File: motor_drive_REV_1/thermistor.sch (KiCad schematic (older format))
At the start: 6 parts, among them J5 Conn_01x02, J6 Conn_01x02

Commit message: started layout
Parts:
- removed C32, C33: 2.2uF, motor_drive_footprints:C_0603_1608Metric, symbol motor_drive:C
- removed J5: Conn_01x02, symbol Connector_Generic:Conn_01x02
- removed R44: 3k, motor_drive_footprints:C_0603_1608Metric, symbol motor_drive:R
- added C43: C, motor_drive_footprints:C_0603_1608Metric, symbol motor_drive:C
- J6: footprint (none) -> motor_drive_footprints:2pos_254
- R43: value 3k -> R
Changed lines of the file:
@@
 $Descr A4 11693 8268
 encoding utf-8
-Sheet 15 15
+Sheet 15 16
 Title ""
 Date ""
@@
 $EndDescr
 $Comp
-L motor_drive:R R44
-U 1 1 5E6227DE
-P 5400 2750
-AR Path="/5E61C379/5E6227DE" Ref="R44"  Part="1"
-AR Path="/5E61FCEC/5E6227DE" Ref="R?"  Part="1"
-AR Path="/5E626DD7/5E6227DE" Ref="R?"  Part="1"
-F 0 "R?" H 5470 2796 50  0000 L CNN
-F 1 "3k" H 5470 2705 50  0000 L CNN
-F 2 "motor_drive_footprints:C_0603_1608Metric" V 5330 2750 50  0001 C CNN
-F 3 "~" H 5400 2750 50  0001 C CNN
-	1    5400 2750
+L motor_drive:R R43
+U 1 1 5E41A8AA
+P 5500 4250
+F 0 "R43" H 5570 4296 50  0000 L CNN
+F 1 "R" H 5570 4205 50  0000 L CNN
+F 2 "motor_drive_footprints:C_0603_1608Metric" V 5430 4250 50  0001 C CNN
+F 3 "~" H 5500 4250 50  0001 C CNN
+	1    5500 4250
 	1    0    0    -1
 $EndComp
 $Comp
-L motor_drive:C C33
-U 1 1 5E6227DF
-P 4500 2750
-AR Path="/5E61C379/5E6227DF" Ref="C33"  Part="1"
-AR Path="/5E61FCEC/5E6227DF" Ref="C?"  Part="1"
-AR Path="/5E626DD7/5E6227DF" Ref="C?"  Part="1"
-F 0 "C?" H 4615 2796 50  0000 L CNN
-F 1 "2.2uF" H 4615 2705 50  0000 L CNN
-F 2 "motor_drive_footprints:C_0603_1608Metric" H 4538 2600 50  0001 C CNN
-F 3 "~" H 4500 2750 50  0001 C CNN
-	1    4500 2750
+L motor_drive:C C43
+U 1 1 5E41AB44
+P 6000 4250
+F 0 "C43" H 6115 4296 50  0000 L CNN
+F 1 "C" H 6115 4205 50  0000 L CNN
+F 2 "motor_drive_footprints:C_0603_1608Metric" H 6038 4100 50  0001 C CNN
+F 3 "~" H 6000 4250 50  0001 C CNN
+	1    6000 4250
 	1    0    0    -1
 $EndComp
 $Comp
 L Connector_Generic:Conn_01x02 J6
-U 1 1 5E6227E0
-P 5200 2200
-AR Path="/5E61C379/5E6227E0" Ref="J6"  Part="1"
-AR Path="/5E61FCEC/5E6227E0" Ref="J?"  Part="1"
-AR Path="/5E626DD7/5E6227E0" Ref="J?"  Part="1"
-F 0 "J?" H 5280 2192 50  0000 L CNN
-F 1 "Conn_01x02" H 5280 2101 50  0000 L CNN
-F 2 "" H 5200 2200 50  0001 C CNN
-F 3 "~" H 5200 2200 50  0001 C CNN
-	1    5200 2200
+U 1 1 5E41B07F
+P 6200 3700
+F 0 "J6" H 6280 3692 50  0000 L CNN
+F 1 "Conn_01x02" H 6280 3601 50  0000 L CNN
+F 2 "motor_drive_footprints:2pos_254" H 6200 3700 50  0001 C CNN
+F 3 "~" H 6200 3700 50  0001 C CNN
+	1    6200 3700
 	1    0    0    -1
 $EndComp
 Wire Wire Line
-	4500 2600 4500 2500
+	5500 3500 6000 3500
 Wire Wire Line
-	4500 2500 5000 2500
+	6000 3500 6000 3700
 Wire Wire Line
-	5000 2500 5000 2600
+	6000 3800 6000 4000
 Wire Wire Line
-	4500 2900 4500 3000
+	5500 4100 5500 4000
 Wire Wire Line
-	4500 3000 5000 3000
+	5500 4000 6000 4000
+Connection ~ 6000 4000
 Wire Wire Line
-	5000 3000 5000 2900
-Text HLabel 4500 3000 0    50   Input ~ 0
+	6000 4000 6000 4100
+Wire Wire Line
+	5500 4400 5500 4500
+Wire Wire Line
+	5500 4500 6000 4500
+Wire Wire Line
+	6000 4500 6000 4400
+Text HLabel 5500 3500 0    50   Input ~ 0
+5.0V
+Text HLabel 5500 4000 0    50   Input ~ 0
+signal
+Text HLabel 5500 4500 0    50   Input ~ 0
 GND
-Text HLabel 4500 2500 0    50   Input ~ 0
-signal
-Text HLabel 4500 2000 0    50   Input ~ 0
-5.0V
-Wire Wire Line
-	4500 2000 5000 2000
-Wire Wire Line
-	5000 2000 5000 2200
-Wire Wire Line
-	5000 2300 5000 2500
-Connection ~ 5000 2500
-$Comp
-L motor_drive:R R?
-U 1 1 5E61C762
-P 5400 2750
-AR Path="/5E61FCEC/5E61C762" Ref="R?"  Part="1"
-AR Path="/5E61C379/5E61C762" Ref="R43"  Part="1"
-AR Path="/5E626DD7/5E61C762" Ref="R?"  Part="1"
-F 0 "R?" H 5470 2796 50  0000 L CNN
-F 1 "3k" H 5470 2705 50  0000 L CNN
-F 2 "motor_drive_footprints:C_0603_1608Metric" V 5330 2750 50  0001 C CNN
-F 3 "~" H 5400 2750 50  0001 C CNN
-	1    5400 2750
-	1    0    0    -1
-$EndComp
-$Comp
-L motor_drive:C C?
-U 1 1 5E61CC30
-P 4500 2750
-AR Path="/5E61FCEC/5E61CC30" Ref="C?"  Part="1"
-AR Path="/5E61C379/5E61CC30" Ref="C32"  Part="1"
-AR Path="/5E626DD7/5E61CC30" Ref="C?"  Part="1"
-F 0 "C?" H 4615 2796 50  0000 L CNN
-F 1 "2.2uF" H 4615 2705 50  0000 L CNN
-F 2 "motor_drive_footprints:C_0603_1608Metric" H 4538 2600 50  0001 C CNN
-F 3 "~" H 4500 2750 50  0001 C CNN
-	1    4500 2750
-	1    0    0    -1
-$EndComp
-$Comp
-L Connector_Generic:Conn_01x02 J?
-U 1 1 5E61D49C
-P 5200 2200
-AR Path="/5E61FCEC/5E61D49C" Ref="J?"  Part="1"
-AR Path="/5E61C379/5E61D49C" Ref="J5"  Part="1"
-AR Path="/5E626DD7/5E61D49C" Ref="J?"  Part="1"
-F 0 "J?" H 5280 2192 50  0000 L CNN
-F 1 "Conn_01x02" H 5280 2101 50  0000 L CNN
-F 2 "" H 5200 2200 50  0001 C CNN
-F 3 "~" H 5200 2200 50  0001 C CNN
-	1    5200 2200
-	1    0    0    -1
-$EndComp
-Text HLabel 4500 3000 0    50   Input ~ 0
-GND
-Text HLabel 4500 2500 0    50   Input ~ 0
-signal
-Text HLabel 4500 2000 0    50   Input ~ 0
-5.0V
 $EndSCHEMATC

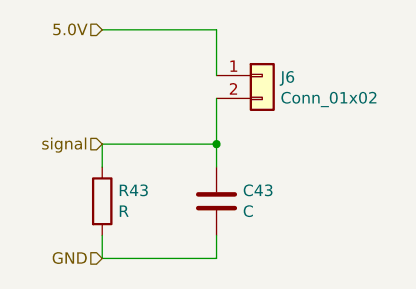
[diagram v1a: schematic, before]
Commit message: gate drive rework and schematic re-organization
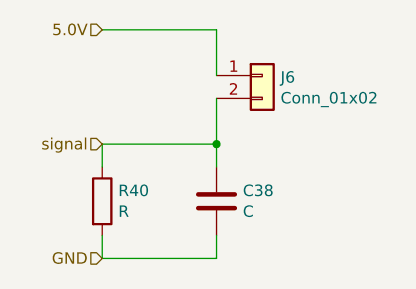
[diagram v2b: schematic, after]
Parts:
- renumbered C43 to C38, R43 to R40
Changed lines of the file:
@@
 $Descr A4 11693 8268
 encoding utf-8
-Sheet 15 16
+Sheet 5 7
 Title ""
 Date ""
@@
 $EndDescr
 $Comp
-L motor_drive:R R43
+L motor_drive:R R40
 U 1 1 5E41A8AA
 P 5500 4250
-F 0 "R43" H 5570 4296 50  0000 L CNN
+F 0 "R40" H 5570 4296 50  0000 L CNN
 F 1 "R" H 5570 4205 50  0000 L CNN
 F 2 "motor_drive_footprints:C_0603_1608Metric" V 5430 4250 50  0001 C CNN
@@
 $EndComp
 $Comp
-L motor_drive:C C43
+L motor_drive:C C38
 U 1 1 5E41AB44
 P 6000 4250
-F 0 "C43" H 6115 4296 50  0000 L CNN
+F 0 "C38" H 6115 4296 50  0000 L CNN
 F 1 "C" H 6115 4205 50  0000 L CNN
 F 2 "motor_drive_footprints:C_0603_1608Metric" H 6038 4100 50  0001 C CNN
